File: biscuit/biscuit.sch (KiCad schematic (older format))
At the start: 63 parts, among them IC1 ATMEGA328-A, P1 D_IN, P2 PWR_IO, P3 UART, P4 ISP, P5 D_OUT, P6 MOT_1, P7 MOT_2, Q1 BC849, Q10 Q_NMOS_DGS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

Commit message: PCB Routing for bisquit
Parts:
- removed Q10, Q4, Q6, Q8: Q_NMOS_DGS, symbol Q_NMOS_DGS
- removed Q3, Q5, Q7, Q9: Q_PMOS_DGS, symbol Q_PMOS_DGS
- removed R13: 10k, symbol R
- removed R14, R15, R16, R17, R18, R19, R20, R21: 1k, symbol R
- added U10, U11, U8, U9: IRF9952, SMD_Packages:SOIC-8-N, symbol IRF9952
- C1, C10, C2, C5, C6, C7, C8, C9: footprint (none) -> Capacitors_SMD:C_0805
- C3, C4: footprint (none) -> Capacitors_Tantalum_SMD:TantalC_SizeA_EIA-3216_Reflow
- D1, D2, D3: footprint (none) -> LEDs:LED_0805
- IC1: footprint TQFP32 -> Housings_QFP:TQFP-32_7x7mm_Pitch0.8mm
- P1, P5: footprint (none) -> Pin_Headers:Pin_Header_Straight_1x08
- P2, P3: footprint (none) -> Pin_Headers:Pin_Header_Straight_1x06
- P4: footprint (none) -> Pin_Headers:Pin_Header_Straight_2x03
- P6, P7: footprint (none) -> Pin_Headers:Pin_Header_Straight_1x04
- Q1, Q2: footprint SOT-23 -> TO_SOT_Packages_SMD:SOT-23
- R1, R10, R11, R12, R2, R22, R23, R3, R4, R5, R6, R7, R8, R9: footprint (none) -> Resistors_SMD:R_0805
- U1, U2: footprint (none) -> SMD_Packages:SO-16-N
- U5, U7: footprint (none) -> SMD_Packages:SOIC-14_N
- U5: renamed from U7; footprint (none) -> SMD_Packages:SOIC-14_N
- U6: footprint (none) -> SMD_Packages:SOIC-8-N
- U7: renamed from U5; footprint (none) -> SMD_Packages:SOIC-14_N
- Y1: footprint (none) -> Crystals:Crystal_HC49-SD_SMD
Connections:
- net +BATT: now also U10.3 (S_PCH), U11.3 (S_PCH), U8.3 (S_PCH), U9.3 (S_PCH)
- net GND: now also U7.11 (V-), U10.1 (S_NCH), U11.1 (S_NCH), U8.1 (S_NCH), U9.1 (S_NCH)
- net MUX_IN: now also IC1.11 ((PCINT23/AIN1)PD7); no longer IC1.1 ((PCINT19/OC2B/INT1)PD3)
- net POWER_HOLD: now also IC1.1 ((PCINT19/OC2B/INT1)PD3); no longer IC1.11 ((PCINT23/AIN1)PD7)
- net V_THH: now also U5.10 (+), U5.12 (+), U7.12 (+); no longer U5.10 (+), U5.3 (+), U7.3 (+)
- net V_THL: now also U5.3 (+), U7.3 (+), U7.5 (+); no longer U5.12 (+), U7.12 (+), U7.5 (+)
- net at C8.1, R12.1: now also U5.13 (-), U5.2 (-); no longer U5.13 (-), U5.9 (-)
- net at P6.3 (P3), P6.4 (P4): now also U8.5 (D2_PCH), U8.6 (D1_PCH), U8.7 (D2_NCH), U8.8 (D1_NCH)
- net at C9.1, R22.1, U5.6 (-): now also U5.9 (-); no longer U5.2 (-)
- net at P6.1 (P1), P6.2 (P2): now also U10.5 (D2_PCH), U10.6 (D1_PCH), U10.7 (D2_NCH), U10.8 (D1_NCH)
- net at U5.7: now also U10.2 (G_NCH)
- net at C7.1, R11.1: now also U7.13 (-), U7.2 (-); no longer U7.2 (-), U7.6 (-)
- net at U7.8: now also U11.4 (G_PCH)
- net at C10.1, R23.1, U7.9 (-): now also U7.6 (-); no longer U7.13 (-)
- net at P7.1 (P1), P7.2 (P2): now also U11.5 (D2_PCH), U11.6 (D1_PCH), U11.7 (D2_NCH), U11.8 (D1_NCH)
- net at P7.3 (P3), P7.4 (P4): now also U9.5 (D2_PCH), U9.6 (D1_PCH), U9.7 (D2_NCH), U9.8 (D1_NCH)
- new net: U5.14, U8.4 (G_PCH)
- new net: U5.1, U8.2 (G_NCH)
- new net: U10.4 (G_PCH), U5.8
- new net: U7.14, U9.4 (G_PCH)
- new net: U7.1, U9.2 (G_NCH)
- new net: U11.2 (G_NCH), U7.7
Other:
- moved on the sheet: C10, C7, C8, C9, P6, P7, R10, R11, R12, R22, R23, R8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

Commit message: First sucessful route for bisquit board
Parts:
- removed P1: D_IN, Pin_Headers:Pin_Header_Straight_1x08, symbol CONN_01X08
- removed P5: D_OUT, Pin_Headers:Pin_Header_Straight_1x08, symbol CONN_01X08
- removed U3: 78L03, symbol 78L05
- added P1: D_IN, Pin_Headers:Pin_Header_Straight_1x09, symbol CONN_01X09
- added P5: D_OUT, Pin_Headers:Pin_Header_Straight_1x09, symbol CONN_01X09
- added U3: TS2940CP33, TO_SOT_Packages_SMD:TO-252-2Lead, symbol TS2940CP33
- SW1: footprint (none) -> custom:Schurter_LSG_1301
- U4: footprint (none) -> custom:RFM75
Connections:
- net +3V3: now also U3.3 (VO)
- net DO_0: now also P5.1 (P1)
- net DO_1: now also P5.2 (P2)
- net DO_2: now also P5.3 (P3)
- net GND: now also P1.9 (P9), P5.9 (P9), U3.2 (GND)
- net RF_IRQ: now also IC1.26 ((PCINT11/ADC3)PC3); no longer IC1.32 ((PCINT18/INT0)PD2)
- net VCC: now also U3.1 (VI)
- net at U2.3 (QD): now also P5.4 (P4)
- net at U2.4 (QE): now also P5.5 (P5)
- net at U2.5 (QF): now also P5.6 (P6)
- net at U2.6 (QG): now also P5.7 (P7)
- net at U2.7 (QH): now also P5.8 (P8)
- net at U1.1 (I3): now also P1.4 (P4)
- net at U1.12 (I7): now also P1.8 (P8)
- net at U1.13 (I6): now also P1.7 (P7)
- net at U1.14 (I5): now also P1.6 (P6)
- net at U1.15 (I4): now also P1.5 (P5)
- net at U1.2 (I2): now also P1.3 (P3)
- net at U1.3 (I1): now also P1.2 (P2)
- net at U1.4 (I0): now also P1.1 (P1)
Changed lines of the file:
@@
 	1    0    0    -1
 $EndComp
-Text Label 1250 9900 2    60   ~ 0
+Text Label 1200 10000 2    60   ~ 0
 MUX_0
-Text Label 1250 10000 2    60   ~ 0
+Text Label 1200 10100 2    60   ~ 0
 MUX_1
-Text Label 1250 10100 2    60   ~ 0
+Text Label 1200 10200 2    60   ~ 0
 MUX_2
-Wire Wire Line
-	1250 9900 1350 9900
-Wire Wire Line
-	1350 10000 1250 10000
-Wire Wire Line
-	1250 10100 1350 10100
 $Comp
 L GND #PWR016
@@
 Wire Wire Line
 	2850 9250 2750 9250
-$Comp
-L CONN_01X08 P1
-U 1 1 5831490B
-P 800 9350
-F 0 "P1" H 800 9800 50  0000 C CNN
-F 1 "D_IN" V 900 9350 50  0000 C CNN
-F 2 "Pin_Headers:Pin_Header_Straight_1x08" H 800 9350 50  0001 C CNN
-F 3 "" H 800 9350 50  0000 C CNN
-	1    800  9350
-	-1   0    0    -1
-$EndComp
 Wire Wire Line
 	1000 9000 1350 9000
@@
 	11350 10000 11250 10000
 $Comp
-L 78L05 U3
-U 1 1 583197A1
-P 5050 1050
-F 0 "U3" H 5200 854 50  0000 C CNN
-F 1 "78L03" H 5050 1250 50  0000 C CNN
-F 2 "" H 5050 1050 50  0001 C CNN
-F 3 "" H 5050 1050 50  0000 C CNN
-	1    5050 1050
-	1    0    0    -1
-$EndComp
-$Comp
 L GND #PWR019
 U 1 1 58319921
@@
 F 0 "U4" H 7350 10150 60  0000 C CNN
 F 1 "RFM75" H 7800 9800 60  0000 C CNN
-F 2 "" H 7700 9800 60  0001 C CNN
+F 2 "custom:RFM75" H 7700 9800 60  0001 C CNN
 F 3 "" H 7700 9800 60  0000 C CNN
 	1    7700 9800
@@
 Text Label 5300 10200 2    60   ~ 0
 DO_0
-$Comp
-L CONN_01X08 P5
-U 1 1 58315F96
-P 6000 9400
-F 0 "P5" H 6000 9850 50  0000 C CNN
-F 1 "D_OUT" V 6100 9400 50  0000 C CNN
-F 2 "Pin_Headers:Pin_Header_Straight_1x08" H 6000 9400 50  0001 C CNN
-F 3 "" H 6000 9400 50  0000 C CNN
-	1    6000 9400
-	1    0    0    -1
-$EndComp
 Wire Wire Line
 	5800 9550 5350 9550
@@
 Text Label 4700 6150 0    60   ~ 0
 RF_CE
-Text Label 4700 5950 0    60   ~ 0
+Text Label 4650 5300 0    60   ~ 0
 RF_IRQ
 $Comp
@@
 	1    0    0    -1
 $EndComp
-Wire Wire Line
-	4700 5950 4550 5950
 Wire Wire Line
 	4700 6150 4550 6150
@@
 F 0 "SW1" H 3150 2510 50  0000 C CNN
 F 1 "SW_PWR" V 3000 2750 50  0000 C CNN
-F 2 "" H 3000 2400 50  0001 C CNN
+F 2 "custom:Schurter_LSG_1301" H 3000 2400 50  0001 C CNN
 F 3 "" H 3000 2400 50  0000 C CNN
 	1    3000 2400
@@
 	10900 1600 11000 1600
 Connection ~ 11000 1600
+$Comp
+L CONN_01X09 P1
+U 1 1 58440D40
+P 800 9400
+F 0 "P1" H 800 9900 50  0000 C CNN
+F 1 "D_IN" V 900 9400 50  0000 C CNN
+F 2 "Pin_Headers:Pin_Header_Straight_1x09" H 800 9400 50  0001 C CNN
+F 3 "" H 800 9400 50  0000 C CNN
+	1    800  9400
+	-1   0    0    -1
+$EndComp
+Wire Wire Line
+	1200 10200 1300 10200
+Wire Wire Line
+	1300 10200 1300 10100
+Wire Wire Line
+	1300 10100 1350 10100
+Wire Wire Line
+	1200 10100 1250 10100
+Wire Wire Line
+	1250 10100 1250 10000
+Wire Wire Line
+	1250 10000 1350 10000
+Wire Wire Line
+	1200 10000 1200 9900
+Wire Wire Line
+	1200 9900 1350 9900
+$Comp
+L GND #PWR054
+U 1 1 58441676
+P 1150 9800
+F 0 "#PWR054" H 1150 9550 50  0001 C CNN
+F 1 "GND" H 1150 9650 50  0000 C CNN
+F 2 "" H 1150 9800 50  0000 C CNN
+F 3 "" H 1150 9800 50  0000 C CNN
+	1    1150 9800
+	0    -1   -1   0
+$EndComp
+Wire Wire Line
+	1150 9800 1000 9800
+$Comp
+L CONN_01X09 P5
+U 1 1 58441C49
+P 6000 9450
+F 0 "P5" H 6000 9950 50  0000 C CNN
+F 1 "D_OUT" V 6100 9450 50  0000 C CNN
+F 2 "Pin_Headers:Pin_Header_Straight_1x09" H 6000 9450 50  0001 C CNN
+F 3 "" H 6000 9450 50  0000 C CNN
+	1    6000 9450
+	1    0    0    -1
+$EndComp
+$Comp
+L GND #PWR055
+U 1 1 58441D06
+P 5650 9850
+F 0 "#PWR055" H 5650 9600 50  0001 C CNN
+F 1 "GND" H 5650 9700 50  0000 C CNN
+F 2 "" H 5650 9850 50  0000 C CNN
+F 3 "" H 5650 9850 50  0000 C CNN
+	1    5650 9850
+	0    1    1    0
+$EndComp
+Wire Wire Line
+	5650 9850 5800 9850
+$Comp
+L TS2940CP33 U3
+U 1 1 58442ADD
+P 5050 1050
+F 0 "U3" H 5200 854 50  0000 C CNN
+F 1 "TS2940CP33" H 5050 1250 50  0000 C CNN
+F 2 "TO_SOT_Packages_SMD:TO-252-2Lead" H 5050 1050 50  0001 C CNN
+F 3 "" H 5050 1050 50  0000 C CNN
+	1    5050 1050
+	1    0    0    -1
+$EndComp
+Wire Wire Line
+	4650 5300 4550 5300
 $EndSCHEMATC

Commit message: Cleanup labels and add power LED
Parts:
- added D4: LED, LEDs:LED_0805, symbol LED
- added R13: 1k, Resistors_SMD:R_0805, symbol R
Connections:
- net +3V3: now also R13.2
- net GND: now also D4.1 (K)
- new net: D4.2 (A), R13.1
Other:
- moved on the sheet: C10, C7, C8, C9, P6, P7, R11, R12, R22, R23, U10, U11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

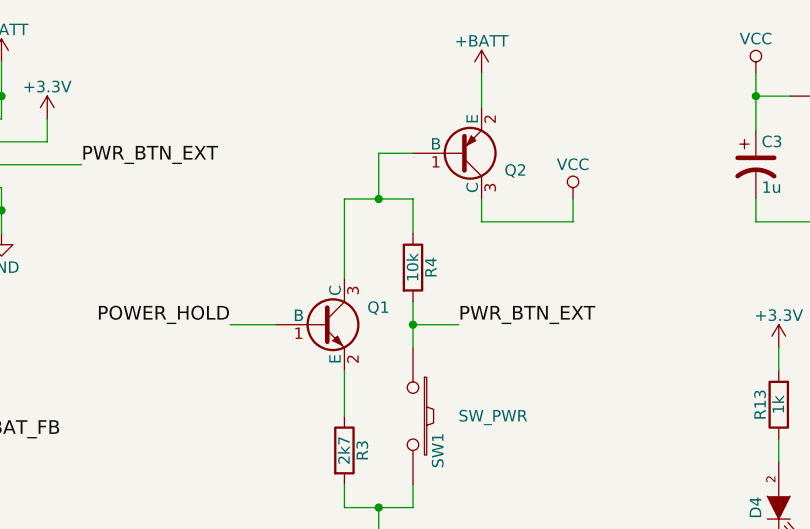
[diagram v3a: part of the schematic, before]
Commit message: Added reference to website
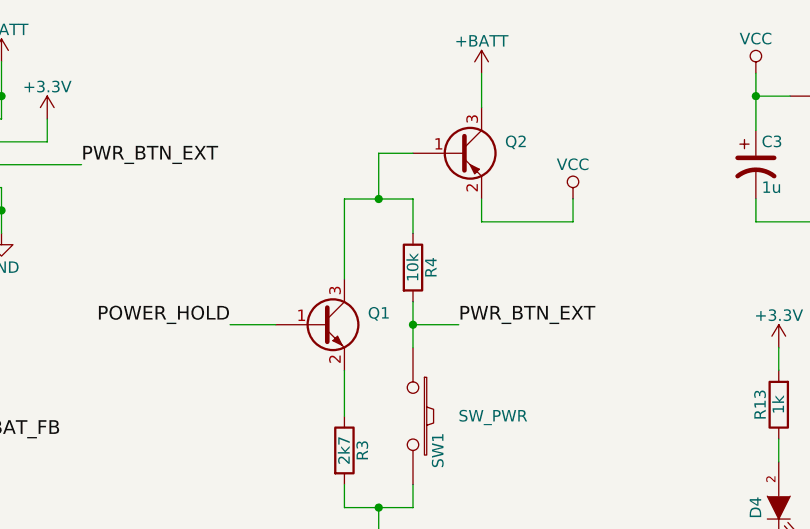
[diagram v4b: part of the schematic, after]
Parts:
- removed Q1: BC849, TO_SOT_Packages_SMD:SOT-23, symbol BC849
- removed Q2: BC856, TO_SOT_Packages_SMD:SOT-23, symbol BC856
- added Q1: Q_NPN_BEC, TO_SOT_Packages_SMD:SOT-23, symbol Q_NPN_BEC
- added Q2: Q_PNP_BEC, TO_SOT_Packages_SMD:SOT-23, symbol Q_PNP_BEC
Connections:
- net +BATT: now also Q2.3 (C)
- net POWER_HOLD: now also Q1.1 (B)
- net VCC: now also Q2.2 (E)
- net at R3.1: now also Q1.2 (E)
- net at R4.1: now also Q1.3 (C), Q2.1 (B)
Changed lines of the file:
@@
 POWER_HOLD
-$Comp
-L BC849 Q1
-U 1 1 58322452
-P 2600 2000
-F 0 "Q1" H 2800 2075 50  0000 L CNN
-F 1 "BC849" H 2800 2000 50  0001 L CNN
-F 2 "TO_SOT_Packages_SMD:SOT-23" H 2800 1925 50  0001 L CIN
-F 3 "" H 2600 2000 50  0000 L CNN
-	1    2600 2000
-	1    0    0    -1
-$EndComp
-$Comp
-L BC856 Q2
-U 1 1 58322543
-P 3200 1250
-F 0 "Q2" H 3400 1325 50  0000 L CNN
-F 1 "BC856" H 3400 1250 50  0001 L CNN
-F 2 "TO_SOT_Packages_SMD:SOT-23" H 3400 1175 50  0001 L CIN
-F 3 "" H 3200 1250 50  0000 L CNN
-	1    3200 1250
-	1    0    0    1
-$EndComp
 $Comp
 L VCC #PWR045
@@
 Wire Wire Line
 	4600 2200 4600 2100
+$Comp
+L Q_NPN_BEC Q1
+U 1 1 58444D14
+P 2600 2000
+F 0 "Q1" H 2900 2050 50  0000 R CNN
+F 1 "Q_NPN_BEC" H 3200 1950 50  0001 R CNN
+F 2 "TO_SOT_Packages_SMD:SOT-23" H 2800 2100 50  0001 C CNN
+F 3 "" H 2600 2000 50  0000 C CNN
+	1    2600 2000
+	1    0    0    -1
+$EndComp
+$Comp
+L Q_PNP_BEC Q2
+U 1 1 58444F02
+P 3200 1250
+F 0 "Q2" H 3500 1300 50  0000 R CNN
+F 1 "Q_PNP_BEC" H 3800 1200 50  0001 R CNN
+F 2 "TO_SOT_Packages_SMD:SOT-23" H 3400 1350 50  0001 C CNN
+F 3 "" H 3200 1250 50  0000 C CNN
+	1    3200 1250
+	1    0    0    -1
+$EndComp
 $EndSCHEMATC
